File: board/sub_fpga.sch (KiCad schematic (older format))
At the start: 0 parts

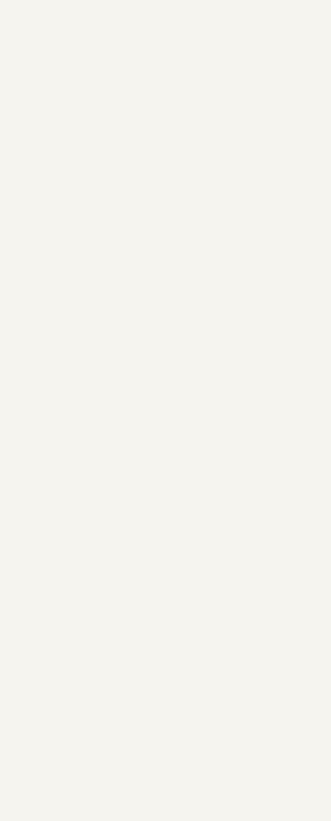
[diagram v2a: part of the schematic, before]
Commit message: More progress on the schematic. 6502 Done.
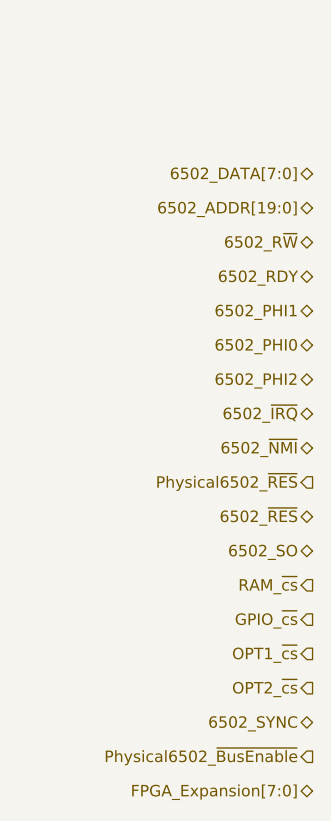
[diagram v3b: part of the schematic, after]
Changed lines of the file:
@@
 $Descr A4 11693 8268
 encoding utf-8
-Sheet 5 8
+Sheet 9 10
 Title ""
 Date ""
@@
 Text HLabel 2150 1350 0    50   Input ~ 0
 KBD_row[0:4]
+Text HLabel 2650 4750 0    50   3State ~ 0
+6502_DATA[7:0]
+Text HLabel 2650 4900 0    50   BiDi ~ 0
+6502_ADDR[19:0]
+Text HLabel 2650 5050 0    50   BiDi ~ 0
+6502_R~W
+Text HLabel 2650 5200 0    50   BiDi ~ 0
+6502_RDY
+Text HLabel 2650 5350 0    50   BiDi ~ 0
+6502_PHI1
+Text HLabel 2650 5500 0    50   BiDi ~ 0
+6502_PHI0
+Text HLabel 2650 5650 0    50   BiDi ~ 0
+6502_PHI2
+Text HLabel 2650 5800 0    50   BiDi ~ 0
+6502_~IRQ
+Text HLabel 2650 5950 0    50   BiDi ~ 0
+6502_~NMI
+Text HLabel 2650 6100 0    50   Output ~ 0
+Physical6502_~RES
+Text HLabel 2650 6400 0    50   BiDi ~ 0
+6502_SO
+Text HLabel 2650 6550 0    50   Output ~ 0
+RAM_~cs
+Text HLabel 2650 6700 0    50   Output ~ 0
+GPIO_~cs
+Text HLabel 2650 6850 0    50   Output ~ 0
+OPT1_~cs
+Text HLabel 2650 7000 0    50   Output ~ 0
+OPT2_~cs
+Text HLabel 2650 7150 0    50   BiDi ~ 0
+6502_SYNC
+Text HLabel 2650 6250 0    50   BiDi ~ 0
+6502_~RES
+Text HLabel 2650 7300 0    50   Output ~ 0
+Physical6502_~BusEnable
+Text HLabel 2650 7450 0    50   BiDi ~ 0
+FPGA_Expansion[7:0]
 $EndSCHEMATC

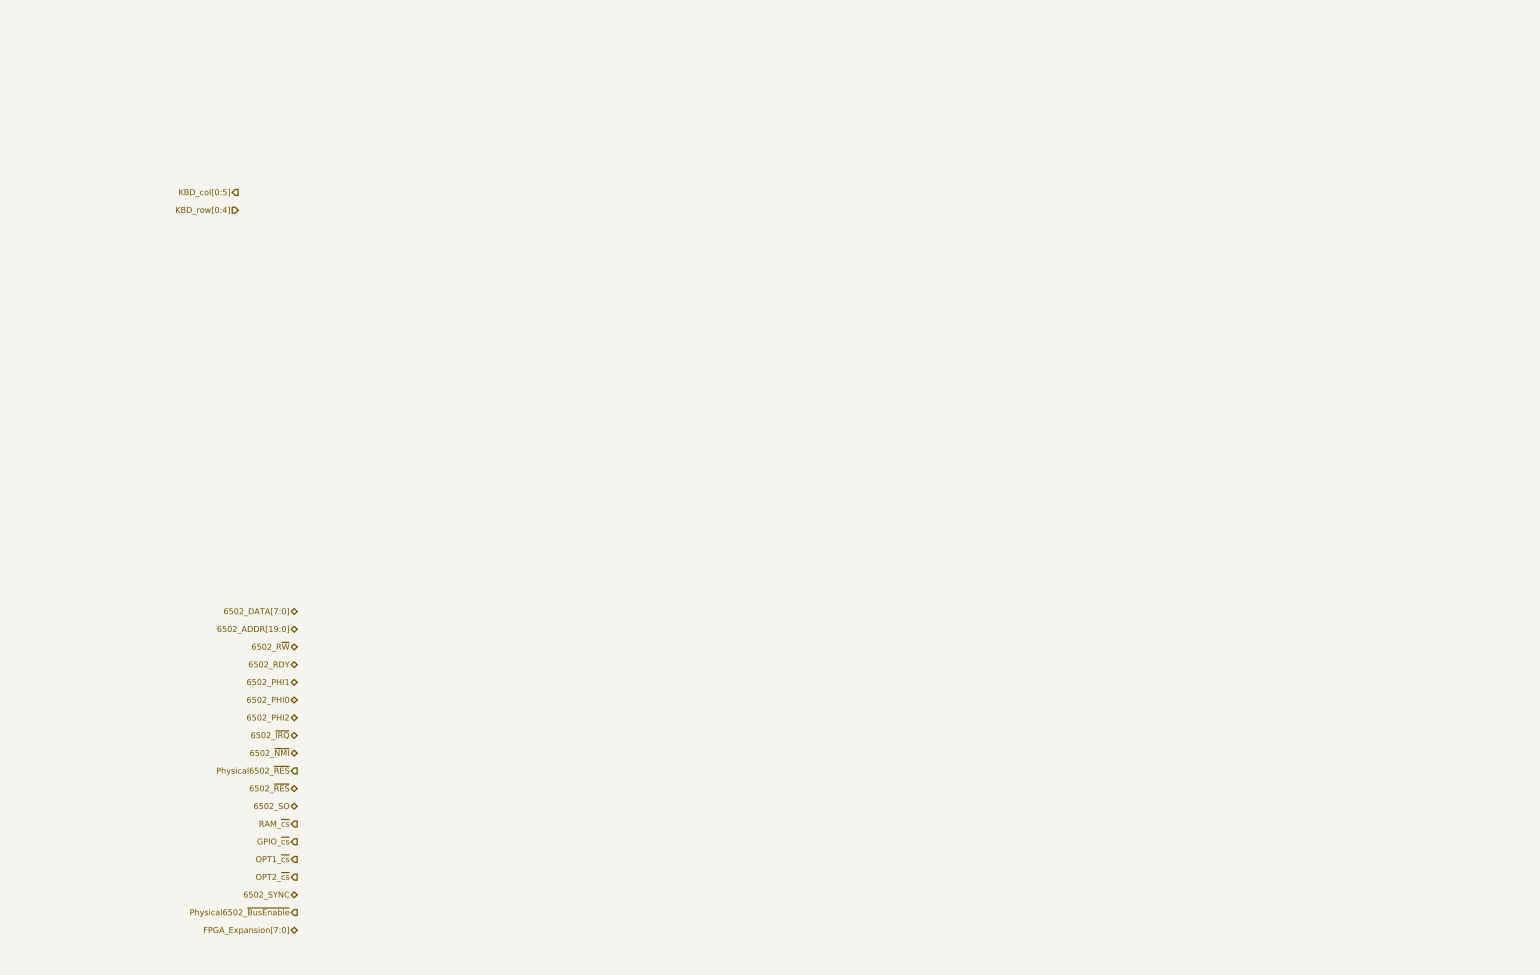
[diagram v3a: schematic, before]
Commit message: Level converters complete, display almost done
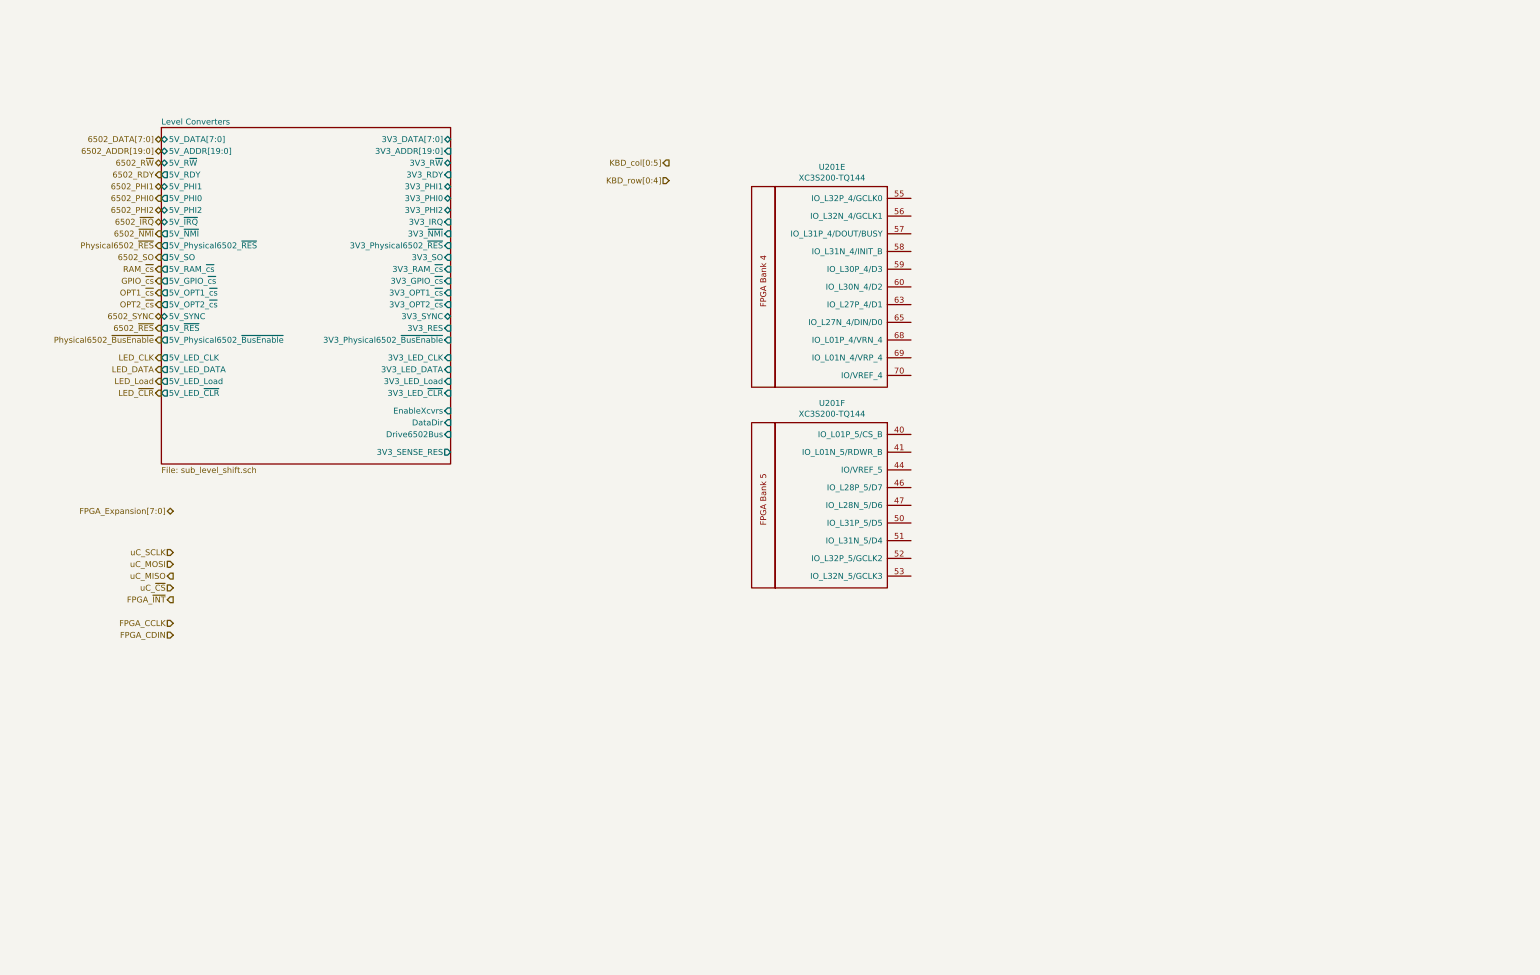
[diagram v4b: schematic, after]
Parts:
- added U201: XC3S200-TQ144, symbol quokka:XC3S200-TQ144
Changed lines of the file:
@@
 $Descr A4 11693 8268
 encoding utf-8
-Sheet 9 10
+Sheet 14 15
 Title ""
 Date ""
@@
 Comment2 ""
 Comment3 ""
-Comment4 ""
+Comment4 "Quokka 6502 Microprocessor Trainer"
 $EndDescr
-Text HLabel 2150 1200 0    50   Output ~ 0
+Text HLabel 5800 950  0    50   Output ~ 0
 KBD_col[0:5]
-Text HLabel 2150 1350 0    50   Input ~ 0
+Text HLabel 5800 1100 0    50   Input ~ 0
 KBD_row[0:4]
-Text HLabel 2650 4750 0    50   3State ~ 0
+Text HLabel 1500 750  0    50   3State ~ 0
 6502_DATA[7:0]
-Text HLabel 2650 4900 0    50   BiDi ~ 0
+Text HLabel 1500 850  0    50   BiDi ~ 0
 6502_ADDR[19:0]
-Text HLabel 2650 5050 0    50   BiDi ~ 0
+Text HLabel 1500 950  0    50   BiDi ~ 0
 6502_R~W
-Text HLabel 2650 5200 0    50   BiDi ~ 0
+Text HLabel 1500 1050 0    50   Output ~ 0
 6502_RDY
-Text HLabel 2650 5350 0    50   BiDi ~ 0
+Text HLabel 1500 1150 0    50   BiDi ~ 0
 6502_PHI1
-Text HLabel 2650 5500 0    50   BiDi ~ 0
+Text HLabel 1500 1250 0    50   Output ~ 0
 6502_PHI0
-Text HLabel 2650 5650 0    50   BiDi ~ 0
+Text HLabel 1500 1350 0    50   BiDi ~ 0
 6502_PHI2
-Text HLabel 2650 5800 0    50   BiDi ~ 0
+Text HLabel 1500 1450 0    50   BiDi ~ 0
 6502_~IRQ
-Text HLabel 2650 5950 0    50   BiDi ~ 0
+Text HLabel 1500 1550 0    50   Output ~ 0
 6502_~NMI
-Text HLabel 2650 6100 0    50   Output ~ 0
+Text HLabel 1500 1650 0    50   Output ~ 0
 Physical6502_~RES
-Text HLabel 2650 6400 0    50   BiDi ~ 0
+Text HLabel 1500 1750 0    50   Output ~ 0
 6502_SO
-Text HLabel 2650 6550 0    50   Output ~ 0
+Text HLabel 1500 1850 0    50   Output ~ 0
 RAM_~cs
-Text HLabel 2650 6700 0    50   Output ~ 0
+Text HLabel 1500 1950 0    50   Output ~ 0
 GPIO_~cs
-Text HLabel 2650 6850 0    50   Output ~ 0
+Text HLabel 1500 2050 0    50   Output ~ 0
 OPT1_~cs
-Text HLabel 2650 7000 0    50   Output ~ 0
+Text HLabel 1500 2150 0    50   Output ~ 0
 OPT2_~cs
-Text HLabel 2650 7150 0    50   BiDi ~ 0
+Text HLabel 1500 2250 0    50   BiDi ~ 0
 6502_SYNC
-Text HLabel 2650 6250 0    50   BiDi ~ 0
+Text HLabel 1500 2350 0    50   Output ~ 0
 6502_~RES
-Text HLabel 2650 7300 0    50   Output ~ 0
+Text HLabel 1500 2450 0    50   Output ~ 0
 Physical6502_~BusEnable
-Text HLabel 2650 7450 0    50   BiDi ~ 0
+Text HLabel 1600 3900 0    50   BiDi ~ 0
 FPGA_Expansion[7:0]
+$Sheet
+S 1500 650  2450 2850
+U 5ACF6640
+F0 "Level Converters" 50
+F1 "sub_level_shift.sch" 50
+F2 "5V_DATA[7:0]" T L 1500 750 50
+F3 "5V_ADDR[19:0]" B L 1500 850 50
+F4 "5V_R~W" B L 1500 950 50
+F5 "5V_RDY" O L 1500 1050 50
+F6 "5V_PHI1" B L 1500 1150 50
+F7 "5V_PHI0" O L 1500 1250 50
+F8 "5V_PHI2" B L 1500 1350 50
+F9 "5V_~IRQ" T L 1500 1450 50
+F10 "5V_~NMI" O L 1500 1550 50
+F11 "5V_Physical6502_~RES" O L 1500 1650 50
+F12 "5V_SO" O L 1500 1750 50
+F13 "5V_RAM_~cs" O L 1500 1850 50
+F14 "5V_GPIO_~cs" O L 1500 1950 50
+F15 "5V_OPT1_~cs" O L 1500 2050 50
+F16 "5V_OPT2_~cs" O L 1500 2150 50
+F17 "5V_SYNC" B L 1500 2250 50
+F18 "5V_~RES" O L 1500 2350 50
+F19 "5V_Physical6502_~BusEnable" O L 1500 2450 50
+F20 "3V3_DATA[7:0]" T R 3950 750 50
+F21 "3V3_ADDR[19:0]" I R 3950 850 50
+F22 "3V3_R~W" B R 3950 950 50
+F23 "3V3_RDY" I R 3950 1050 50
+F24 "3V3_PHI1" B R 3950 1150 50
+F25 "3V3_PHI0" B R 3950 1250 50
+F26 "3V3_PHI2" B R 3950 1350 50
+F27 "3V3_~NMI" I R 3950 1550 50
+F28 "3V3_Physical6502_~RES" I R 3950 1650 50
+F29 "3V3_SO" I R 3950 1750 50
+F30 "3V3_RAM_~cs" I R 3950 1850 50
+F31 "3V3_GPIO_~cs" I R 3950 1950 50
+F32 "3V3_OPT1_~cs" I R 3950 2050 50
+F33 "3V3_OPT2_~cs" I R 3950 2150 50
+F34 "3V3_SYNC" B R 3950 2250 50
+F35 "3V3_Physical6502_~BusEnable" I R 3950 2450 50
+F36 "5V_LED_CLK" O L 1500 2600 50
+F37 "5V_LED_DATA" O L 1500 2700 50
+F38 "5V_LED_Load" O L 1500 2800 50
+F39 "EnableXcvrs" I R 3950 3050 50
+F40 "Drive6502Bus" I R 3950 3250 50
+F41 "DataDir" I R 3950 3150 50
+F42 "3V3_LED_CLK" I R 3950 2600 50
+F43 "3V3_LED_DATA" I R 3950 2700 50
+F44 "3V3_LED_Load" I R 3950 2800 50
+F45 "3V3_LED_~CLR" I R 3950 2900 50
+F46 "5V_LED_~CLR" O L 1500 2900 50
+F47 "3V3_IRQ" I R 3950 1450 50
+F48 "3V3_RES" I R 3950 2350 50
+F49 "3V3_SENSE_RES" O R 3950 3400 50
+$EndSheet
+Text HLabel 1500 2600 0    50   Output ~ 0
+LED_CLK
+Text HLabel 1500 2700 0    50   Output ~ 0
+LED_DATA
+Text HLabel 1500 2800 0    50   Output ~ 0
+LED_Load
+Text HLabel 1600 4250 0    50   Input ~ 0
+uC_SCLK
+Text HLabel 1600 4350 0    50   Input ~ 0
+uC_MOSI
+Text HLabel 1600 4450 0    50   Output ~ 0
+uC_MISO
+Text HLabel 1600 4550 0    50   Input ~ 0
+uC_~CS
+Text HLabel 1600 4650 0    50   Output ~ 0
+FPGA_~INT
+Text HLabel 1600 4850 0    50   Input ~ 0
+FPGA_CCLK
+Text HLabel 1600 4950 0    50   Input ~ 0
+FPGA_CDIN
+Text HLabel 1500 2900 0    50   Output ~ 0
+LED_~CLR
+$Comp
+L quokka:XC3S200-TQ144 U201
+U 5 1 5AB59013
+P 7400 1900
+F 0 "U201" H 7181 2815 50  0000 C CNN
+F 1 "XC3S200-TQ144" H 7181 2724 50  0000 C CNN
+F 2 "" H 6950 2000 50  0001 C CNN
+F 3 "" H 6950 2000 50  0001 C CNN
+	5    7400 1900
+	1    0    0    -1
+$EndComp
+$Comp
+L quokka:XC3S200-TQ144 U201
+U 6 1 5AB59047
+P 7250 3900
+F 0 "U201" H 7181 4815 50  0000 C CNN
+F 1 "XC3S200-TQ144" H 7181 4724 50  0000 C CNN
+F 2 "" H 6800 4000 50  0001 C CNN
+F 3 "" H 6800 4000 50  0001 C CNN
+	6    7250 3900
+	1    0    0    -1
+$EndComp
 $EndSCHEMATC

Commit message: More Schematic progress
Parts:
- added U? (x2): XC3S200-TQ144, symbol quokka:XC3S200-TQ144
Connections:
- new net A0: U?.108 (IO_L01N_2/VRP_2)
- new net A1: U?.107 (IO_L01P_2/VRN_2)
- new net A10: U?.96 (IO_L24N_2)
- new net A11: U?.95 (IO_L24P_2)
- new net A12: U?.93 (IO_L40N_2)
- new net A13: U?.92 (IO_L40P_2/VREF_2)
- new net A14: U?.90 (IO_L40N_3/VREF_3)
- new net A15: U?.89 (IO_L40P_3)
- new net A16: U?.87 (IO_L24N_3)
- new net A17: U?.86 (IO_L24P_3)
- new net A18: U?.85 (IO_L23N_3)
- new net A19: U?.84 (IO_L23P_3/VREF_3)
- new net A2: U?.105 (IO_L20N_2)
- new net A3: U?.104 (IO_L20P_2)
- new net A4: U?.103 (IO_L21N_2)
- new net A5: U?.102 (IO_L21P_2)
- new net A6: U?.100 (IO_L22N_2)
- new net A7: U?.99 (IO_L22P_2)
- new net A8: U?.98 (IO_L23N_2/VREF_2)
- new net A9: U?.97 (IO_L23P_2)
- new net D0: U?.73 (IO_L01P_3/VRN_3)
- new net D1: U?.74 (IO_L01N_3/VRP_3)
- new net D2: U?.76 (IO)
- new net D3: U?.77 (IO_L20P_3)
- new net D4: U?.78 (IO_L20N_3)
- new net D5: U?.79 (IO_L21P_3)
- new net D6: U?.80 (IO_L21N_3)
- new net D7: U?.82 (IO_L22P_3)
- no-connect marks 0 -> 1
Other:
- moved on the sheet: U201E, U201F
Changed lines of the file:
@@
 $Descr A4 11693 8268
 encoding utf-8
-Sheet 14 15
+Sheet 13 14
 Title ""
 Date ""
@@
 Comment4 "Quokka 6502 Microprocessor Trainer"
 $EndDescr
-Text HLabel 5800 950  0    50   Output ~ 0
+Text HLabel 5950 -300 0    50   Output ~ 0
 KBD_col[0:5]
-Text HLabel 5800 1100 0    50   Input ~ 0
+Text HLabel 5950 -150 0    50   Input ~ 0
 KBD_row[0:4]
 Text HLabel 1500 750  0    50   3State ~ 0
@@
 L quokka:XC3S200-TQ144 U201
 U 5 1 5AB59013
-P 7400 1900
-F 0 "U201" H 7181 2815 50  0000 C CNN
-F 1 "XC3S200-TQ144" H 7181 2724 50  0000 C CNN
-F 2 "" H 6950 2000 50  0001 C CNN
-F 3 "" H 6950 2000 50  0001 C CNN
-	5    7400 1900
+P 12650 3550
+F 0 "U201" H 12431 4465 50  0000 C CNN
+F 1 "XC3S200-TQ144" H 12431 4374 50  0000 C CNN
+F 2 "" H 12200 3650 50  0001 C CNN
+F 3 "" H 12200 3650 50  0001 C CNN
+	5    12650 3550
 	1    0    0    -1
 $EndComp
@@
 L quokka:XC3S200-TQ144 U201
 U 6 1 5AB59047
-P 7250 3900
-F 0 "U201" H 7181 4815 50  0000 C CNN
-F 1 "XC3S200-TQ144" H 7181 4724 50  0000 C CNN
-F 2 "" H 6800 4000 50  0001 C CNN
-F 3 "" H 6800 4000 50  0001 C CNN
-	6    7250 3900
+P 12500 5700
+F 0 "U201" H 12431 6615 50  0000 C CNN
+F 1 "XC3S200-TQ144" H 12431 6524 50  0000 C CNN
+F 2 "" H 12050 5800 50  0001 C CNN
+F 3 "" H 12050 5800 50  0001 C CNN
+	6    12500 5700
 	1    0    0    -1
 $EndComp
+$Comp
+L quokka:XC3S200-TQ144 U?
+U 4 1 5B2B027C
+P 10350 2050
+F 0 "U?" H 10206 2965 50  0000 C CNN
+F 1 "XC3S200-TQ144" H 10206 2874 50  0000 C CNN
+F 2 "" H 9900 2150 50  0001 C CNN
+F 3 "" H 9900 2150 50  0001 C CNN
+	4    10350 2050
+	1    0    0    -1
+$EndComp
+$Comp
+L quokka:XC3S200-TQ144 U?
+U 3 1 5B2B02B6
+P 10350 4650
+F 0 "U?" H 10206 5565 50  0000 C CNN
+F 1 "XC3S200-TQ144" H 10206 5474 50  0000 C CNN
+F 2 "" H 9900 4750 50  0001 C CNN
+F 3 "" H 9900 4750 50  0001 C CNN
+	3    10350 4650
+	1    0    0    -1
+$EndComp
+Wire Bus Line
+	3950 850  9400 850
+Entry Wire Line
+	11000 5000 10900 4900
+Entry Wire Line
+	11000 5150 10900 5050
+Entry Wire Line
+	11000 5300 10900 5200
+Entry Wire Line
+	11000 5450 10900 5350
+Entry Wire Line
+	11000 5600 10900 5500
+Entry Wire Line
+	11000 5750 10900 5650
+Entry Wire Line
+	11000 5900 10900 5800
+Entry Wire Line
+	11000 6050 10900 5950
+Text Label 10900 5950 2    50   ~ 0
+A0
+Text Label 10900 5800 2    50   ~ 0
+A1
+Text Label 10900 5650 2    50   ~ 0
+A2
+Text Label 10900 5500 2    50   ~ 0
+A3
+Text Label 10900 5350 2    50   ~ 0
+A4
+Text Label 10900 5200 2    50   ~ 0
+A5
+Text Label 10900 5050 2    50   ~ 0
+A6
+Text Label 10900 4900 2    50   ~ 0
+A7
+Wire Wire Line
+	10800 5350 10900 5350
+Wire Wire Line
+	10900 5200 10800 5200
+Wire Wire Line
+	10800 5050 10900 5050
+Wire Wire Line
+	10900 4900 10800 4900
+Wire Wire Line
+	10900 5950 10800 5950
+Wire Wire Line
+	10800 5800 10900 5800
+Wire Wire Line
+	10900 5650 10800 5650
+Wire Wire Line
+	10800 5500 10900 5500
+Wire Wire Line
+	10800 4750 10900 4750
+Wire Wire Line
+	10900 4600 10800 4600
+Wire Wire Line
+	10800 4450 10900 4450
+Wire Wire Line
+	10900 4300 10800 4300
+Wire Wire Line
+	10800 4150 10900 4150
+Wire Wire Line
+	10900 4000 10800 4000
+Wire Wire Line
+	10800 3500 10900 3500
+Wire Wire Line
+	10900 3350 10800 3350
+Text Label 10900 4750 2    50   ~ 0
+A8
+Text Label 10900 4600 2    50   ~ 0
+A9
+Text Label 10900 4450 2    50   ~ 0
+A10
+Text Label 10900 4300 2    50   ~ 0
+A11
+Text Label 10900 3350 2    50   ~ 0
+A15
+Text Label 10900 3500 2    50   ~ 0
+A14
+Text Label 10900 4000 2    50   ~ 0
+A13
+Text Label 10900 4150 2    50   ~ 0
+A12
+Entry Wire Line
+	11000 3450 10900 3350
+Entry Wire Line
+	11000 3600 10900 3500
+Entry Wire Line
+	11000 4100 10900 4000
+Entry Wire Line
+	11000 4250 10900 4150
+Entry Wire Line
+	11000 4400 10900 4300
+Entry Wire Line
+	11000 4550 10900 4450
+Entry Wire Line
+	11000 4700 10900 4600
+Entry Wire Line
+	11000 4850 10900 4750
+Entry Wire Line
+	11000 3300 10900 3200
+Entry Wire Line
+	11000 3150 10900 3050
+Entry Wire Line
+	11000 3000 10900 2900
+Entry Wire Line
+	11000 2850 10900 2750
+Text Label 10900 2750 2    50   ~ 0
+A19
+Text Label 10900 2900 2    50   ~ 0
+A18
+Text Label 10900 3050 2    50   ~ 0
+A17
+Text Label 10900 3200 2    50   ~ 0
+A16
+Wire Wire Line
+	10900 2750 10800 2750
+Wire Wire Line
+	10800 2900 10900 2900
+Wire Wire Line
+	10900 3050 10800 3050
+Wire Wire Line
+	10800 3200 10900 3200
+Entry Wire Line
+	10900 2450 11000 2350
+Entry Wire Line
+	10900 2300 11000 2200
+Entry Wire Line
+	10900 2150 11000 2050
+Entry Wire Line
+	10900 2000 11000 1900
+Entry Wire Line
+	10900 1850 11000 1750
+Entry Wire Line
+	10900 1700 11000 1600
+Entry Wire Line
+	10900 1550 11000 1450
+Entry Wire Line
+	10900 1400 11000 1300
+Text Label 10900 1400 2    50   ~ 0
+D0
+Text Label 10900 1550 2    50   ~ 0
+D1
+Text Label 10900 1700 2    50   ~ 0
+D2
+Text Label 10900 1850 2    50   ~ 0
+D3
+Text Label 10900 2000 2    50   ~ 0
+D4
+Text Label 10900 2150 2    50   ~ 0
+D5
+Text Label 10900 2300 2    50   ~ 0
+D6
+Text Label 10900 2450 2    50   ~ 0
+D7
+Wire Wire Line
+	10800 2450 10900 2450
+Wire Wire Line
+	10900 2300 10800 2300
+Wire Wire Line
+	10800 2150 10900 2150
+Wire Wire Line
+	10900 2000 10800 2000
+Wire Wire Line
+	10800 1850 10900 1850
+Wire Wire Line
+	10900 1700 10800 1700
+Wire Wire Line
+	10800 1550 10900 1550
+Wire Wire Line
+	10900 1400 10800 1400
+NoConn ~ 10800 2600
+Wire Bus Line
+	3950 750  11000 750
+Wire Bus Line
+	11000 6300 9400 6300
+Wire Bus Line
+	9400 850  9400 6300
+Wire Bus Line
+	11000 750  11000 2350
+Wire Bus Line
+	11000 2850 11000 6300
+Text Label 6300 750  0    50   ~ 0
+D[0:7]
+Text Label 6300 850  0    50   ~ 0
+A[0:19]
 $EndSCHEMATC
